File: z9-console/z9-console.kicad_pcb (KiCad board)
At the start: 2 copper layers, 89.5 x 55.5 mm, 130 parts, among them J10 Screw_Terminal_01x06, J2 LCD 3.2" 240x320 Conn_01x14_P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, J4 Conn_01x04_Pin, J6 ST_STDC14 - SAMTEC_FTSH-107-0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, J7 TC2070 - TAG Connect, J801 USB_C_Receptacle_USB2.0_16P, J9 JST GH, Q701 AO3400A, SW2 SW_Push, SW3 SW_Push, U11 ST_SENSOR_2, U2 TPS22919DCKR, U3 SN74LVC1G14DRLR, U5 TLV76733DRVx, U6 B0505XT-1WR3, U7 LMR14006YDDCR, U8 STM32F427V_G-I_Tx, U9 ISM330DHCX, U951 ISO1042-Q1, X2 8MHz 20pF

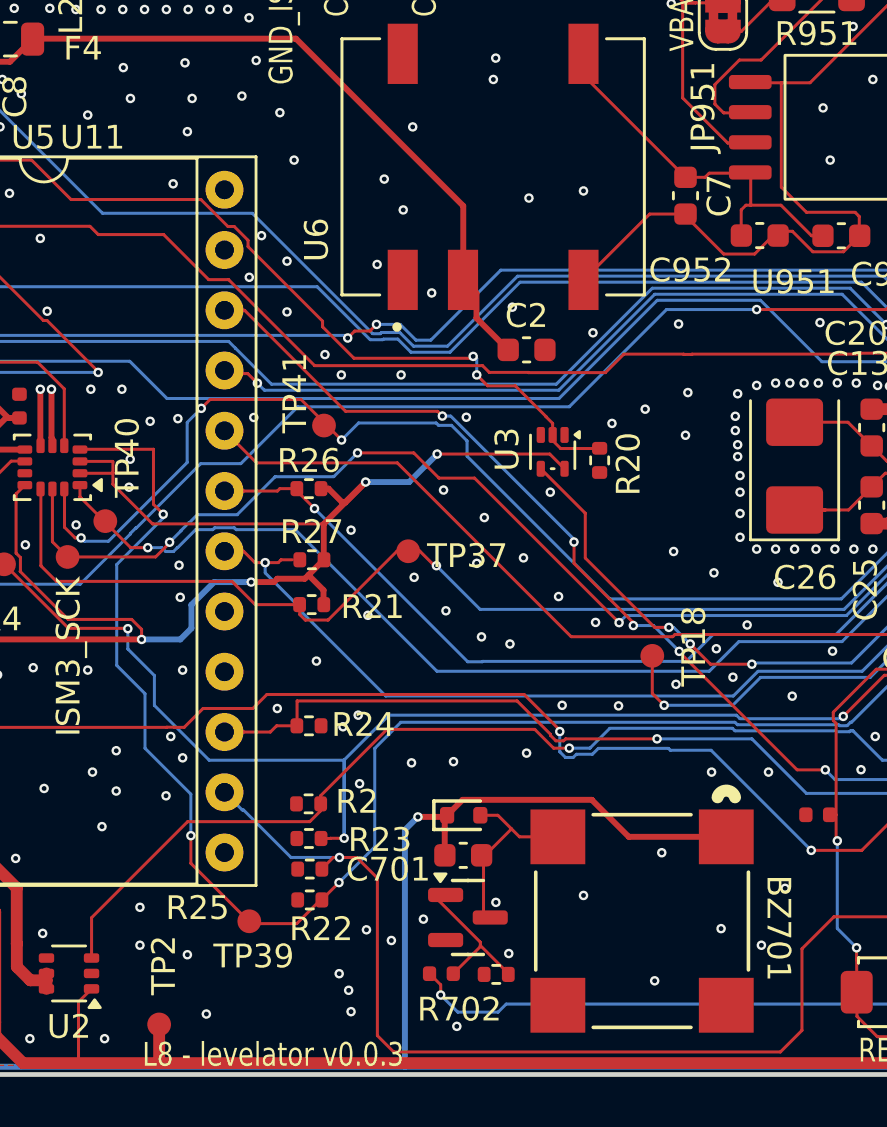
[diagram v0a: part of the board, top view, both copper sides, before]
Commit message: Update schematic and project configuration
- Changed the starting number for annotation in the project configuration from 300 to 700.
- Removed the "+5V_ISO" label from the schematic.
- Adjusted the position of the "PE13" label.
- Added a new "VBATT" label in the schematic.
- Updated the "shared buzzer" sheet reference, changing its UUID and properties.
- Modified the pin configuration for the "BUZZER" input in the schematic.
- Cleaned up unused labels and adjusted pin placements for clarity.
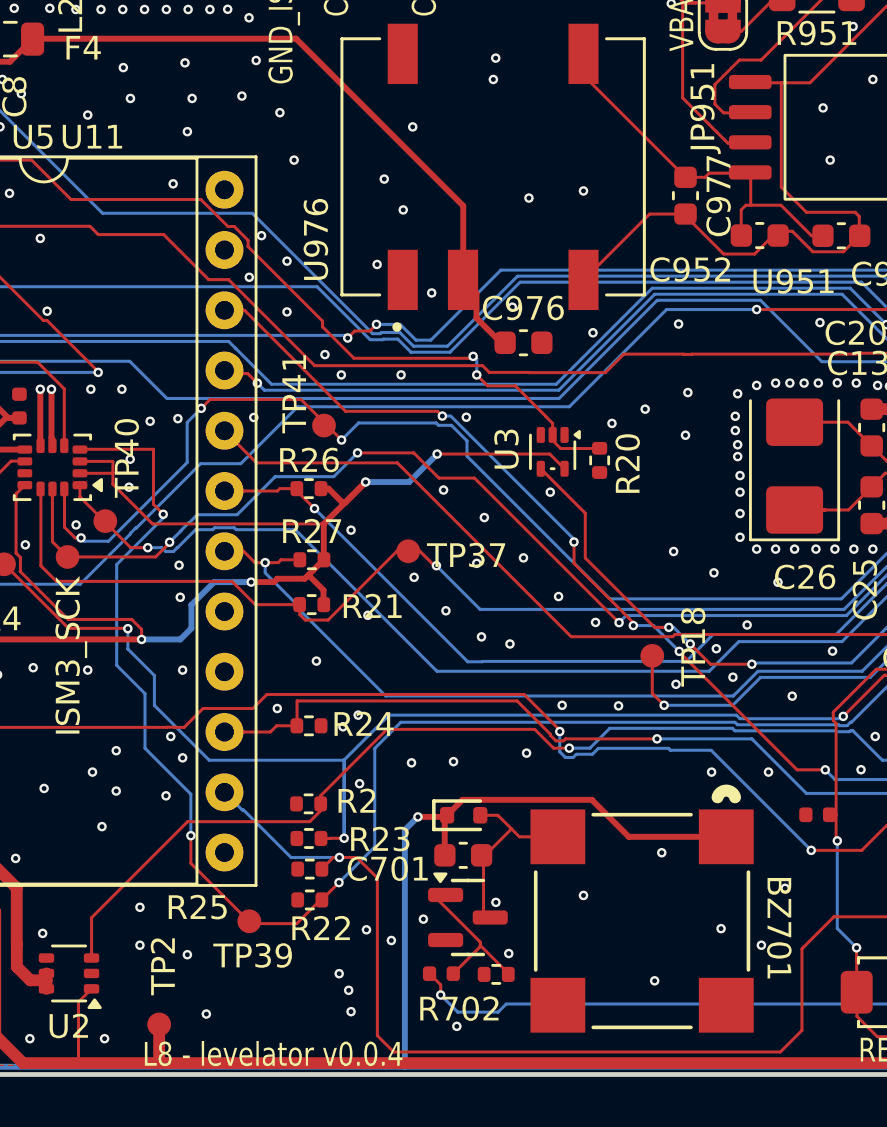
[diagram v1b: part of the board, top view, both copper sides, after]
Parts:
- moved C976 0.33 mm to (121.7, 96.5)
- renumbered C2 to C976, C7 to C977, U6 to U976
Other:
- board text added: "L8 - levelator v0.0.4"
- board text removed: "L8 - levelator v0.0.3"

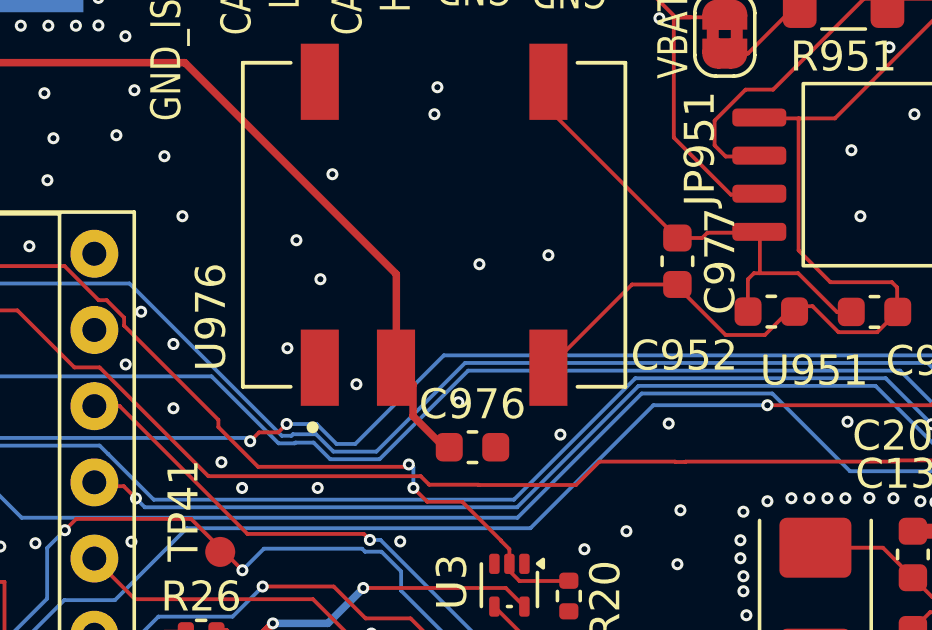
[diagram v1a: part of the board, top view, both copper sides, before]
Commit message: Update reference designators and adjust USB label positions for consistency
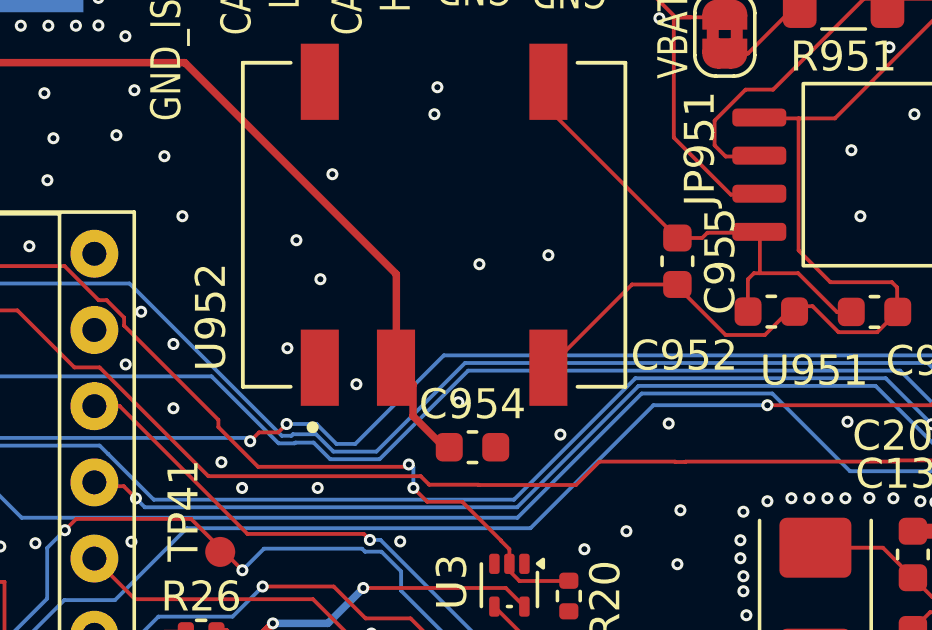
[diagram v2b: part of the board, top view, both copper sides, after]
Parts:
- renumbered C976 to C954, C977 to C955, U976 to U952
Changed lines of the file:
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@@
 		(descr "Capacitor SMD 0603 (1608 Metric), square (rectangular) end terminal, IPC-7351 nominal, (Body size source: IPC-SM-782 page 76, https://www.pcb-3d.com/wordpress/wp-content/uploads/ipc-sm-782a_amendment_1_and_2.pdf), generated with kicad-footprint-generator")
 		(tags "capacitor")
-		(property "Reference" "C976"
+		(property "Reference" "C954"
 			(at 0 -1.43 0)
 			(layer "F.SilkS")
@@
 		(layer "F.Cu")
 		(at 120.38 89.045 90)
-		(property "Reference" "U976"
+		(property "Reference" "U952"
 			(at -3.075 -7.435 90)
 			(layer "F.SilkS")
@@
 		(descr "Capacitor SMD 0603 (1608 Metric), square (rectangular) end terminal, IPC-7351 nominal, (Body size source: IPC-SM-782 page 76, https://www.pcb-3d.com/wordpress/wp-content/uploads/ipc-sm-782a_amendment_1_and_2.pdf), generated with kicad-footprint-generator")
 		(tags "capacitor")
-		(property "Reference" "C977"
+		(property "Reference" "C955"
 			(at 0 -1.43 90)
 			(layer "F.SilkS")

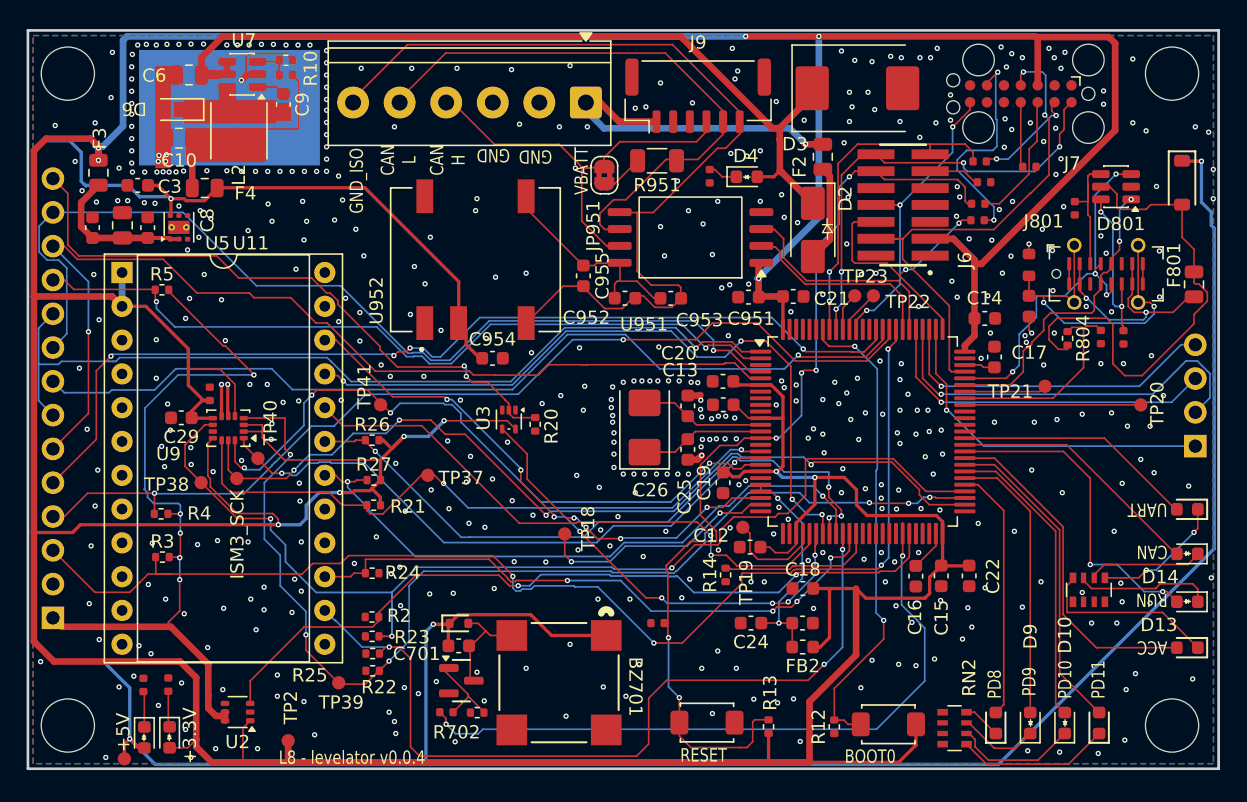
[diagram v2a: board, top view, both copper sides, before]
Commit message: Update KiCad project files and schematic references
- Changed active layer in z9-console.kicad_prl from 5 to 0.
- Removed a missing courtyard warning from z9-console.kicad_pro.
- Updated library footprint mismatch handling from ignore to error in z9-console.kicad_pro.
- Changed net conflict handling from warning to error in z9-console.kicad_pro.
- Updated silk over copper and silk overlap handling from warning to ignore in z9-console.kicad_pro.
- Changed via dangling handling from warning to error in z9-console.kicad_pro.
- Updated reference properties in shared_isolated_can.kicad_sch, changing several references from #PWR0954 and #PWR0955 to #PWR0105 and #PWR0106 respectively, and added project paths for new references.
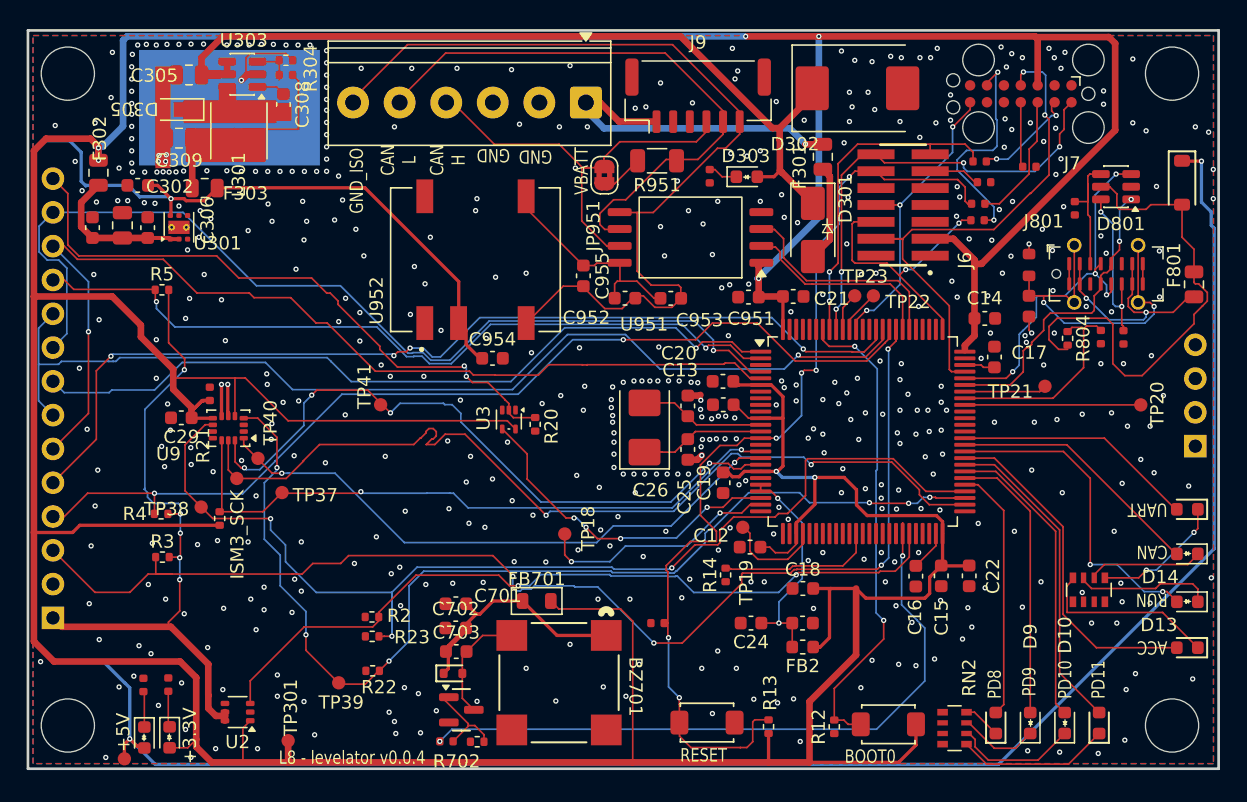
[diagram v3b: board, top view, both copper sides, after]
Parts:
- removed R24, R25, R26, R27: 10K, dnt:R_0402_1005Metric
- removed U11: ST_SENSOR_2, dnt:DIP-24_W15.24mm_Socket- nox
- added C702: 100nF, dnt:C_0603_1608Metric, F.Cu at (118.9, 116.7)
- added C703: 100nF, dnt:C_0603_1608Metric, F.Cu at (118.9, 118.5)
- added FB701: ~, dnt:F_0805_2012Metric, F.Cu at (125.0, 114.7)
- C701: value 100nF -> 10uF
- moved R21 11.6 mm to (101.2, 108.5), turned to -90 degrees
- moved TP37 11.0 mm to (105.8, 106.5)
- moved D701 3.79 mm to (118.7, 120.1)
- moved C701 3.17 mm to (118.9, 114.9), turned to 180 degrees
- moved Q701 2.19 mm to (119.3, 122.9)
- moved R701 2.19 mm to (118.2, 125.2)
- moved R702 2.19 mm to (120.5, 125.3)
- moved TP38 1.84 mm to (99.8, 107.6)
- renumbered C3 to C302, C4 to C303, C5 to C304, C6 to C305, C8 to C306, C9 to C308, C10 to C309, D2 to D301, D3 to D302, D4 to D303, D5 to D304, D6 to D305, D7 to D306, F2 to F301, F3 to F302, F4 to F303, L2 to L301, R7 to R301, R8 to R302, R9 to R303, R10 to R304, R11 to R305, TP2 to TP301, TP3 to TP302, U5 to U301, U7 to U303
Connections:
- BZ701 pad 1: +5V -> Net-(BZ701-+)
- C701 pad 1: +5V -> Net-(BZ701-+)
- C701 pad 2: Net-(BZ701--) -> GND
- D701 pad 1: +5V -> Net-(BZ701-+)
- J4 pad 1: /SPI3_CS -> unconnected-(J4-Pin_1-Pad1)
- J4 pad 2: /SPI3_SDI -> unconnected-(J4-Pin_2-Pad2)
- J4 pad 3: /SPI3_SDO -> unconnected-(J4-Pin_3-Pad3)
- J4 pad 4: /SPI3_SCK -> unconnected-(J4-Pin_4-Pad4)
- U8 pad 30: /SPI1_SCK -> /MCU/SPI1_SCK
- U8 pad 31: /SPI1_SDI -> /MCU/SPI1_SDI
- U8 pad 32: /SPI1_SDO -> /MCU/SPI1_SDO
- U8 pad 33: /SPI1_CS -> /MCU/SPI1_CS
- U8 pad 34: /SPI1_CS2 -> /MCU/SPI1_CS2
- U8 pad 35: /SPI1_IRQ -> /MCU/SPI1_IRQ
- U8 pad 36: /SPI1_IRQ2 -> /MCU/SPI1_IRQ2
- U8 pad 77: /SPI3_CS -> /MCU/SPI3_CS
- U8 pad 78: /SPI3_SCK -> /MCU/SPI3_SCK
- U8 pad 79: /SPI3_SDI -> /MCU/SPI3_SDI
- U8 pad 80: /SPI3_SDO -> /MCU/SPI3_SDO
- U9 pad 11: +3.3V -> unconnected-(U9-SDO_AUX-Pad11)
- U9 pad 2: +3.3V -> unconnected-(U9-SDx-Pad2)
- U9 pad 3: +3.3V -> unconnected-(U9-SCx-Pad3)
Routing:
- net /SPI1_IRQ: track 62.3 -> 0.00 mm, vias 3 -> 0
- net /SPI1_SDO: track 53.2 -> 0.00 mm, vias 4 -> 0
- net /SPI1_CS: track 49.8 -> 0.00 mm, vias 4 -> 0
- net /SPI1_SDI: track 49.8 -> 0.00 mm, vias 8 -> 0
- net /SPI1_CS2: track 47.2 -> 0.00 mm, vias 2 -> 0
- net /SPI1_IRQ2: track 45.9 -> 0.00 mm, vias 4 -> 0
- net /SPI1_SCK: track 43.8 -> 0.00 mm, vias 2 -> 0
- net /SPI3_SDI: track 30.6 -> 0.00 mm, vias 1 -> 0
- net /SPI3_CS: track 26.2 -> 0.00 mm, vias 1 -> 0
- net +5V: track 247.2 -> 221.0 mm, vias 4 -> 3
- net /SPI3_SDO: track 26.1 -> 0.00 mm, vias 1 -> 0
- net /SPI3_SCK: track 25.0 -> 0.00 mm, vias 1 -> 0
- net Net-(BZ701-+): track 0.00 -> 20.4 mm
- net +3.3V: track 455.8 -> 440.1 mm, vias 11 -> 7
- net Net-(J2-VCC): track 57.8 -> 50.1 mm
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
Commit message: mainly route vip
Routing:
- net +3.3V: track 440.1 -> 439.6 mm
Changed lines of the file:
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@@
+	)
+	(segment
+		(start 149.72001 114.49)
+		(end 154.16 114.49)
+		(width 0.25)
+		(layer "F.Cu")
+		(net 2)
+	)
+	(segment
+		(start 99.03 100.15)
+		(end 97.66 98.78)
+		(width 0.5)
+		(layer "F.Cu")
+		(net 2)
+	)
+	(segment
+		(start 102.3 100.8)
+		(end 102.3 97.94)
+		(width 0.127127)
+		(layer "F.Cu")
+		(net 2)
+	)
+	(segment
+		(start 141.665 89.535)
+		(end 141.890001 89.309999)
+		(width 0.5)
+		(layer "F.Cu")
+		(net 2)
+	)
+	(segment
+		(start 91.45 79.95)
+		(end 88.1 79.95)
+		(width 0.5)
+		(layer "F.Cu")
+		(net 2)
+	)
+	(segment
+		(start 168.465 79.313646)
+		(end 158.418646 89.36)
+		(width 0.5)
+		(layer "F.Cu")
+		(net 2)
+	)
+	(segment
+		(start 97.39 125.735)
+		(end 98.75541 125.735)
+		(width 0.127127)
+		(layer "F.Cu")
+		(net 2)
+	)
+	(segment
+		(start 168.465 72.785)
+		(end 168.465 79.313646)
+		(width 0.5)
+		(layer "F.Cu")
+		(net 2)
+	)
+	(segment
+		(start 141.665 91.86)
+		(end 141.665 89.535)
+		(width 0.5)
+		(layer "F.Cu")
+		(net 2)
+	)
+	(segment
+		(start 148.99 113.75999)
+		(end 148.99 118.76)
+		(width 0.5)
+		(layer "F.Cu")
+		(net 2)
+	)
+	(segment
+		(start 153.490225 123.970225)
+		(end 153.490225 125.530225)
+		(width 0.25)
+		(layer "F.Cu")
+		(net 2)
+	)
+	(segment
+		(start 158.418646 89.36)
+		(end 157.89 89.36)
+		(width 0.5)
+		(layer "F.Cu")
+		(net 2)
+	)
+	(segment
+		(start 87.190225 109.55)
+		(end 87.190225 117.740225)
+		(width 0.5)
+		(layer "F.Cu")
+		(net 2)
+	)
+	(segment
+		(start 126.0425 114.7)
+		(end 126.6425 115.3)
+		(width 0.127127)
+		(layer "F.Cu")
+		(net 2)
+	)
+	(segment
+		(start 126.6425 115.3)
+		(end 131.29 115.3)
+		(width 0.127127)
+		(layer "F.Cu")
+		(net 2)
+	)
+	(segment
+		(start 157.89 94.76)
+		(end 157.89 93.46)
+		(width 0.5)
+		(layer "F.Cu")
+		(net 2)
+	)
+	(segment
+		(start 88.7 119.25)
+		(end 98.18 119.25)
+		(width 0.5)
+		(layer "F.Cu")
+		(net 2)
+	)
+	(segment
+		(start 122.769415 101.151915)
+		(end 123.39 101.7725)
+		(width 0.127127)
+		(layer "F.Cu")
+		(net 2)
+	)
+	(segment
+		(start 99.0125 100.9625)
+		(end 100.6375 100.9625)
+		(width 0.25)
+		(layer "F.Cu")
+		(net 2)
+	)
+	(segment
+		(start 143.854999 111.07)
+		(end 142.92 111.07)
+		(width 0.127127)
+		(layer "F.Cu")
+		(net 2)
+	)
+	(segment
+		(start 87.190225 117.740225)
+		(end 88.7 119.25)
+		(width 0.5)
+		(layer "F.Cu")
+		(net 2)
+	)
+	(segment
+		(start 148.99 118.76)
+		(end 145.49 122.26)
+		(width 0.5)
+		(layer "F.Cu")
+		(net 2)
+	)
+	(segment
+		(start 92.04 80.64)
+		(end 92.04 80.54)
+		(width 0.5)
+		(layer "F.Cu")
+		(net 2)
+	)
+	(segment
+		(start 132.2 126.830816)
+		(end 142.410225 126.830816)
+		(width 0.5)
+		(layer "F.Cu")
+		(net 2)
+	)
+	(segment
+		(start 144.49 109.635)
+		(end 144.49 110.434999)
+		(width 0.127127)
+		(layer "F.Cu")
+		(net 2)
 	)
 	(segment
@@
 	)
 	(segment
-		(start 149.72001 114.49)
-		(end 154.16 114.49)
-		(width 0.25)
-		(layer "F.Cu")
-		(net 2)
-	)
-	(segment
-		(start 102.3 100.8)
-		(end 102.3 97.94)
-		(width 0.127127)
-		(layer "F.Cu")
-		(net 2)
-	)
-	(segment
-		(start 141.665 89.535)
-		(end 141.890001 89.309999)
-		(width 0.5)
-		(layer "F.Cu")
-		(net 2)
-	)
-	(segment
-		(start 95.23 93.9659)
-		(end 93.0741 91.81)
-		(width 0.5)
-		(layer "F.Cu")
-		(net 2)
-	)
-	(segment
-		(start 91.45 79.95)
-		(end 88.1 79.95)
-		(width 0.5)
-		(layer "F.Cu")
-		(net 2)
-	)
-	(segment
-		(start 168.465 79.313646)
-		(end 158.418646 89.36)
-		(width 0.5)
-		(layer "F.Cu")
-		(net 2)
-	)
-	(segment
-		(start 97.39 125.735)
-		(end 98.75541 125.735)
-		(width 0.127127)
-		(layer "F.Cu")
-		(net 2)
-	)
-	(segment
-		(start 168.465 72.785)
-		(end 168.465 79.313646)
-		(width 0.5)
-		(layer "F.Cu")
-		(net 2)
-	)
-	(segment
-		(start 141.665 91.86)
-		(end 141.665 89.535)
-		(width 0.5)
-		(layer "F.Cu")
-		(net 2)
-	)
-	(segment
-		(start 148.99 113.75999)
-		(end 148.99 118.76)
-		(width 0.5)
-		(layer "F.Cu")
-		(net 2)
-	)
-	(segment
-		(start 153.490225 123.970225)
-		(end 153.490225 125.530225)
-		(width 0.25)
-		(layer "F.Cu")
-		(net 2)
-	)
-	(segment
-		(start 158.418646 89.36)
-		(end 157.89 89.36)
-		(width 0.5)
-		(layer "F.Cu")
-		(net 2)
-	)
-	(segment
-		(start 87.190225 109.55)
-		(end 87.190225 117.740225)
-		(width 0.5)
-		(layer "F.Cu")
-		(net 2)
-	)
-	(segment
-		(start 126.0425 114.7)
-		(end 126.6425 115.3)
-		(width 0.127127)
-		(layer "F.Cu")
-		(net 2)
-	)
-	(segment
-		(start 126.6425 115.3)
-		(end 131.29 115.3)
-		(width 0.127127)
-		(layer "F.Cu")
-		(net 2)
-	)
-	(segment
-		(start 157.89 94.76)
-		(end 157.89 93.46)
-		(width 0.5)
-		(layer "F.Cu")
-		(net 2)
-	)
-	(segment
-		(start 88.7 119.25)
-		(end 98.18 119.25)
-		(width 0.5)
-		(layer "F.Cu")
-		(net 2)
-	)
-	(segment
-		(start 122.769415 101.151915)
-		(end 123.39 101.7725)
-		(width 0.127127)
-		(layer "F.Cu")
-		(net 2)
-	)
-	(segment
-		(start 99.0125 100.9625)
-		(end 100.6375 100.9625)
-		(width 0.25)
-		(layer "F.Cu")
-		(net 2)
-	)
-	(segment
-		(start 143.854999 111.07)
-		(end 142.92 111.07)
-		(width 0.127127)
-		(layer "F.Cu")
-		(net 2)
-	)
-	(segment
-		(start 87.190225 117.740225)
-		(end 88.7 119.25)
-		(width 0.5)
-		(layer "F.Cu")
-		(net 2)
-	)
-	(segment
-		(start 148.99 118.76)
-		(end 145.49 122.26)
-		(width 0.5)
-		(layer "F.Cu")
-		(net 2)
-	)
-	(segment
-		(start 92.04 80.64)
-		(end 92.04 80.54)
-		(width 0.5)
-		(layer "F.Cu")
-		(net 2)
-	)
-	(segment
-		(start 132.2 126.830816)
-		(end 142.410225 126.830816)
-		(width 0.5)
-		(layer "F.Cu")
-		(net 2)
-	)
-	(segment
-		(start 144.49 109.635)
-		(end 144.49 110.434999)
-		(width 0.127127)
-		(layer "F.Cu")
-		(net 2)
-	)
-	(segment
 		(start 88.1 79.95)
 		(end 87.190225 80.859775)
@@
 	)
 	(segment
-		(start 93.0741 91.81)
-		(end 87.190225 91.81)
+		(start 97.66 98.78)
+		(end 97.66 97.28)
 		(width 0.5)
 		(layer "F.Cu")
@@
 	)
 	(segment
-		(start 95.23 94.85)
-		(end 95.23 93.9659)
-		(width 0.5)
-		(layer "F.Cu")
-		(net 2)
-	)
-	(segment
 		(start 148.98999 113.76)
 		(end 147.09 113.76)
@@
 		(end 146.99 117.46)
 		(width 0.25)
-		(layer "F.Cu")
-		(net 2)
-	)
-	(segment
-		(start 97.66 98.78)
-		(end 97.66 97.28)
-		(width 0.5)
 		(layer "F.Cu")
 		(net 2)
@@
 	)
 	(segment
+		(start 92.19 91.81)
+		(end 87.190225 91.81)
+		(width 0.5)
+		(layer "F.Cu")
+		(net 2)
+	)
+	(segment
 		(start 103.08 97.94)
 		(end 106.291915 101.151915)
@@
 	)
 	(segment
-		(start 99.03 100.15)
-		(end 97.66 98.78)
+		(start 97.66 97.28)
+		(end 92.19 91.81)
 		(width 0.5)
 		(layer "F.Cu")
@@
 		(layer "F.Cu")
 		(net 2)
-	)
-	(segment
-		(start 97.66 97.28)
-		(end 95.23 94.85)
-		(width 0.5)
-		(layer "F.Cu")
-		(net 2)
